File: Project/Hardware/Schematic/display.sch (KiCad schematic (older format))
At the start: 0 parts

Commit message: Skapade LCD symbol och lade till display-krets.
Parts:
- added C?: 2.2u, symbol Device:C
- added LCD?: DEM16228SBH-PW-N, symbol PASC:DEM16228SBH-PW-N
- added Q?: BSS138, Package_TO_SOT_SMD:SOT-23, symbol Transistor_FET:BSS138
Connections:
- net labels added: +5V, GND, LCD_BACKLIGHT, LCD_CONTRAST, LCD_DB0, LCD_DB1, LCD_DB2, LCD_DB3, LCD_DB4, LCD_DB5, LCD_DB6, LCD_DB7, LCD_E, LCD_RS, LCD_RW, LCD_VDD, LCD_VLED, LCD_VSS
- wire segments 0 -> 8
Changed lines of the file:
@@
 EELAYER 26 0
 EELAYER END
-$Descr A4 11693 8268
+$Descr User 5906 5906
 encoding utf-8
-Sheet 1 7
+Sheet 5 7
 Title ""
 Date ""
@@
 Comment4 ""
 $EndDescr
+$Comp
+L PASC:DEM16228SBH-PW-N LCD?
+U 1 1 5C58DC7E
+P 3600 2200
+F 0 "LCD?" H 3927 2246 50  0000 L CNN
+F 1 "DEM16228SBH-PW-N" H 3927 2155 50  0000 L CNN
+F 2 "" H 4000 2500 50  0001 C CNN
+F 3 "" H 4000 2500 50  0001 C CNN
+	1    3600 2200
+	1    0    0    -1
+$EndComp
+Text Label 3200 2900 2    50   ~ 0
+LCD_DB7
+Text Label 3200 2800 2    50   ~ 0
+LCD_DB6
+Text Label 3200 2700 2    50   ~ 0
+LCD_DB5
+Text Label 3200 2600 2    50   ~ 0
+LCD_DB4
+Text Label 3200 2500 2    50   ~ 0
+LCD_DB3
+Text Label 3200 2400 2    50   ~ 0
+LCD_DB2
+Text Label 3200 2300 2    50   ~ 0
+LCD_DB1
+Text Label 3200 2200 2    50   ~ 0
+LCD_DB0
+Text Label 3200 2100 2    50   ~ 0
+LCD_E
+Text Label 3200 2000 2    50   ~ 0
+LCD_RW
+Text Label 3200 1900 2    50   ~ 0
+LCD_RS
+Text Label 3200 1800 2    50   ~ 0
+LCD_CONTRAST
+$Comp
+L power:+5V #PWR?
+U 1 1 5C58DDEB
+P 1800 1500
+F 0 "#PWR?" H 1800 1350 50  0001 C CNN
+F 1 "+5V" H 1815 1673 50  0000 C CNN
+F 2 "" H 1800 1500 50  0001 C CNN
+F 3 "" H 1800 1500 50  0001 C CNN
+	1    1800 1500
+	1    0    0    -1
+$EndComp
+$Comp
+L power:GND #PWR?
+U 1 1 5C58DE2B
+P 1800 2100
+F 0 "#PWR?" H 1800 1850 50  0001 C CNN
+F 1 "GND" H 1805 1927 50  0000 C CNN
+F 2 "" H 1800 2100 50  0001 C CNN
+F 3 "" H 1800 2100 50  0001 C CNN
+	1    1800 2100
+	1    0    0    -1
+$EndComp
+Text Label 3200 1700 2    50   ~ 0
+LCD_VDD
+Text Label 3200 1600 2    50   ~ 0
+LCD_VSS
+Text Label 3200 1500 2    50   ~ 0
+LCD_VLED
+$Comp
+L Device:C C?
+U 1 1 5C58DF2A
+P 1800 1800
+F 0 "C?" H 1915 1846 50  0000 L CNN
+F 1 "2.2u" H 1915 1755 50  0000 L CNN
+F 2 "" H 1838 1650 50  0001 C CNN
+F 3 "~" H 1800 1800 50  0001 C CNN
+	1    1800 1800
+	1    0    0    -1
+$EndComp
+Wire Wire Line
+	1800 1650 1800 1600
+Wire Wire Line
+	1800 1950 1800 2000
+Wire Wire Line
+	1800 1600 2000 1600
+Connection ~ 1800 1600
+Wire Wire Line
+	1800 1600 1800 1500
+Wire Wire Line
+	1800 2000 2000 2000
+Connection ~ 1800 2000
+Wire Wire Line
+	1800 2000 1800 2100
+Text Label 2000 1600 0    50   ~ 0
+LCD_VDD
+Text Label 2000 2000 0    50   ~ 0
+LCD_VSS
+$Comp
+L Transistor_FET:BSS138 Q?
+U 1 1 5C58DFD0
+P 1700 3000
+F 0 "Q?" H 1905 3046 50  0000 L CNN
+F 1 "BSS138" H 1905 2955 50  0000 L CNN
+F 2 "Package_TO_SOT_SMD:SOT-23" H 1900 2925 50  0001 L CIN
+F 3 "https://www.fairchildsemi.com/datasheets/BS/BSS138.pdf" H 1700 3000 50  0001 L CNN
+	1    1700 3000
+	1    0    0    -1
+$EndComp
+Text Label 1500 3000 2    50   ~ 0
+LCD_BACKLIGHT
+$Comp
+L power:GND #PWR?
+U 1 1 5C58E03F
+P 1800 3300
+F 0 "#PWR?" H 1800 3050 50  0001 C CNN
+F 1 "GND" H 1805 3127 50  0000 C CNN
+F 2 "" H 1800 3300 50  0001 C CNN
+F 3 "" H 1800 3300 50  0001 C CNN
+	1    1800 3300
+	1    0    0    -1
+$EndComp
+Wire Wire Line
+	1800 2800 1800 2700
+Text Label 1800 2700 0    50   ~ 0
+LCD_VLED
+Wire Wire Line
+	1800 3200 1800 3300
 $EndSCHEMATC

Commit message: Lade till gate-resistor till LCD-backlight FETen.
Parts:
- added R?: 100, symbol Device:R
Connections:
- wire segments 8 -> 10
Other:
- moved on the sheet: Q?
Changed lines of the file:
@@
 L Transistor_FET:BSS138 Q?
 U 1 1 5C58DFD0
-P 1700 3000
-F 0 "Q?" H 1905 3046 50  0000 L CNN
-F 1 "BSS138" H 1905 2955 50  0000 L CNN
-F 2 "Package_TO_SOT_SMD:SOT-23" H 1900 2925 50  0001 L CIN
-F 3 "https://www.fairchildsemi.com/datasheets/BS/BSS138.pdf" H 1700 3000 50  0001 L CNN
-	1    1700 3000
+P 2000 3000
+F 0 "Q?" H 2205 3046 50  0000 L CNN
+F 1 "BSS138" H 2205 2955 50  0000 L CNN
+F 2 "Package_TO_SOT_SMD:SOT-23" H 2200 2925 50  0001 L CIN
+F 3 "https://www.fairchildsemi.com/datasheets/BS/BSS138.pdf" H 2000 3000 50  0001 L CNN
+	1    2000 3000
 	1    0    0    -1
 $EndComp
-Text Label 1500 3000 2    50   ~ 0
+Text Label 1400 3000 2    50   ~ 0
 LCD_BACKLIGHT
 $Comp
 L power:GND #PWR?
 U 1 1 5C58E03F
-P 1800 3300
-F 0 "#PWR?" H 1800 3050 50  0001 C CNN
-F 1 "GND" H 1805 3127 50  0000 C CNN
-F 2 "" H 1800 3300 50  0001 C CNN
-F 3 "" H 1800 3300 50  0001 C CNN
-	1    1800 3300
+P 2100 3300
+F 0 "#PWR?" H 2100 3050 50  0001 C CNN
+F 1 "GND" H 2105 3127 50  0000 C CNN
+F 2 "" H 2100 3300 50  0001 C CNN
+F 3 "" H 2100 3300 50  0001 C CNN
+	1    2100 3300
 	1    0    0    -1
 $EndComp
 Wire Wire Line
-	1800 2800 1800 2700
-Text Label 1800 2700 0    50   ~ 0
+	2100 2800 2100 2700
+Text Label 2100 2700 0    50   ~ 0
 LCD_VLED
 Wire Wire Line
-	1800 3200 1800 3300
+	2100 3200 2100 3300
+$Comp
+L Device:R R?
+U 1 1 5C58E912
+P 1600 3000
+F 0 "R?" V 1500 3000 50  0000 C CNN
+F 1 "100" V 1700 3000 50  0000 C CNN
+F 2 "" V 1530 3000 50  0001 C CNN
+F 3 "~" H 1600 3000 50  0001 C CNN
+	1    1600 3000
+	0    1    1    0
+$EndComp
+Wire Wire Line
+	1800 3000 1750 3000
+Wire Wire Line
+	1450 3000 1400 3000
 $EndSCHEMATC

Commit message: La till connection stm32 till display, footprint for DEM16220 lcd
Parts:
- removed LCD?: DEM16228SBH-PW-N, symbol PASC:DEM16228SBH-PW-N
- added J?: Conn_01x16_Male, symbol Connector:Conn_01x16_Male
- added U?: DEM16220SYM, symbol PASC:DEM16220SYM
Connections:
- net labels added: LCD_VLED+, LCD_VLED-, LCS_RW, LCS_VDD, V0
- wire segments 10 -> 26
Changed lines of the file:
@@
 $EndDescr
-$Comp
-L PASC:DEM16228SBH-PW-N LCD?
-U 1 1 5C58DC7E
-P 3600 2200
-F 0 "LCD?" H 3927 2246 50  0000 L CNN
-F 1 "DEM16228SBH-PW-N" H 3927 2155 50  0000 L CNN
-F 2 "" H 4000 2500 50  0001 C CNN
-F 3 "" H 4000 2500 50  0001 C CNN
-	1    3600 2200
-	1    0    0    -1
-$EndComp
-Text Label 3200 2900 2    50   ~ 0
-LCD_DB7
-Text Label 3200 2800 2    50   ~ 0
-LCD_DB6
-Text Label 3200 2700 2    50   ~ 0
-LCD_DB5
-Text Label 3200 2600 2    50   ~ 0
-LCD_DB4
-Text Label 3200 2500 2    50   ~ 0
-LCD_DB3
-Text Label 3200 2400 2    50   ~ 0
-LCD_DB2
-Text Label 3200 2300 2    50   ~ 0
-LCD_DB1
-Text Label 3200 2200 2    50   ~ 0
-LCD_DB0
-Text Label 3200 2100 2    50   ~ 0
-LCD_E
-Text Label 3200 2000 2    50   ~ 0
-LCD_RW
-Text Label 3200 1900 2    50   ~ 0
-LCD_RS
-Text Label 3200 1800 2    50   ~ 0
-LCD_CONTRAST
 $Comp
 L power:+5V #PWR?
@@
 	1    0    0    -1
 $EndComp
-Text Label 3200 1700 2    50   ~ 0
-LCD_VDD
-Text Label 3200 1600 2    50   ~ 0
-LCD_VSS
-Text Label 3200 1500 2    50   ~ 0
-LCD_VLED
 $Comp
 L Device:C C?
@@
 Wire Wire Line
 	1450 3000 1400 3000
+$Comp
+L Connector:Conn_01x16_Male J?
+U 1 1 5C69769F
+P 3200 2250
+F 0 "J?" H 3306 3128 50  0000 C CNN
+F 1 "Conn_01x16_Male" H 3306 3037 50  0000 C CNN
+F 2 "" H 3200 2250 50  0001 C CNN
+F 3 "~" H 3200 2250 50  0001 C CNN
+	1    3200 2250
+	-1   0    0    1
+$EndComp
+Wire Wire Line
+	3000 2950 2600 2950
+Text Label 2600 2950 0    50   ~ 0
+LCD_VSS
+Wire Wire Line
+	3000 2850 2600 2850
+Text Label 2600 2850 0    50   ~ 0
+LCD_VDD
+Wire Wire Line
+	3000 2750 2600 2750
+Text Label 2600 2750 0    50   ~ 0
+V0
+Wire Wire Line
+	3000 2650 2600 2650
+Text Label 2600 2650 0    50   ~ 0
+LCD_RS
+Wire Wire Line
+	3000 2550 2600 2550
+Text Label 2600 2550 0    50   ~ 0
+LCS_RW
+Wire Wire Line
+	3000 2450 2600 2450
+Text Label 2600 2450 0    50   ~ 0
+LCD_E
+Wire Wire Line
+	3000 2350 2600 2350
+Text Label 2600 2350 0    50   ~ 0
+LCD_DB0
+Wire Wire Line
+	3000 2250 2600 2250
+Text Label 2600 2250 0    50   ~ 0
+LCD_DB1
+Wire Wire Line
+	3000 2150 2600 2150
+Text Label 2600 2150 0    50   ~ 0
+LCD_DB2
+Wire Wire Line
+	3000 2050 2600 2050
+Text Label 2600 2050 0    50   ~ 0
+LCD_DB3
+Wire Wire Line
+	3000 1950 2600 1950
+Text Label 2600 1950 0    50   ~ 0
+LCD_DB4
+Wire Wire Line
+	3000 1850 2600 1850
+Text Label 2600 1850 0    50   ~ 0
+LCD_DB5
+Wire Wire Line
+	3000 1750 2600 1750
+Text Label 2600 1750 0    50   ~ 0
+LCD_DB6
+Wire Wire Line
+	3000 1650 2600 1650
+Text Label 2600 1650 0    50   ~ 0
+LCD_DB7
+Wire Wire Line
+	3000 1550 2600 1550
+Wire Wire Line
+	3000 1450 2600 1450
+Text Label 2600 1550 0    50   ~ 0
+LCD_VLED+
+Text Label 2600 1450 0    50   ~ 0
+LCD_VLED-
+$Comp
+L PASC:DEM16220SYM U?
+U 1 1 5C69A8D5
+P 4500 2000
+F 0 "U?" H 4827 1946 50  0000 L CNN
+F 1 "DEM16220SYM" H 4827 1855 50  0000 L CNN
+F 2 "" H 4500 2000 50  0001 C CNN
+F 3 "" H 4500 2000 50  0001 C CNN
+	1    4500 2000
+	1    0    0    -1
+$EndComp
+Text Label 4100 1350 2    50   ~ 0
+LCD_VSS
+Text Label 4100 1450 2    50   ~ 0
+LCS_VDD
+Text Label 4100 1550 2    50   ~ 0
+LCD_CONTRAST
+Text Label 4100 1650 2    50   ~ 0
+LCD_RS
+Text Label 4100 1750 2    50   ~ 0
+LCD_RW
+Text Label 4100 1850 2    50   ~ 0
+LCD_E
+Text Label 4100 1950 2    50   ~ 0
+LCD_DB0
+Text Label 4100 2050 2    50   ~ 0
+LCD_DB1
+Text Label 4100 2150 2    50   ~ 0
+LCD_DB2
+Text Label 4100 2250 2    50   ~ 0
+LCD_DB3
+Text Label 4100 2350 2    50   ~ 0
+LCD_DB4
+Text Label 4100 2450 2    50   ~ 0
+LCD_DB5
+Text Label 4100 2550 2    50   ~ 0
+LCD_DB6
+Text Label 4100 2650 2    50   ~ 0
+LCD_DB7
+Text Label 4100 2800 2    50   ~ 0
+LCD_VLED+
+Text Label 4100 2900 2    50   ~ 0
+LCD_VLED-
 $EndSCHEMATC

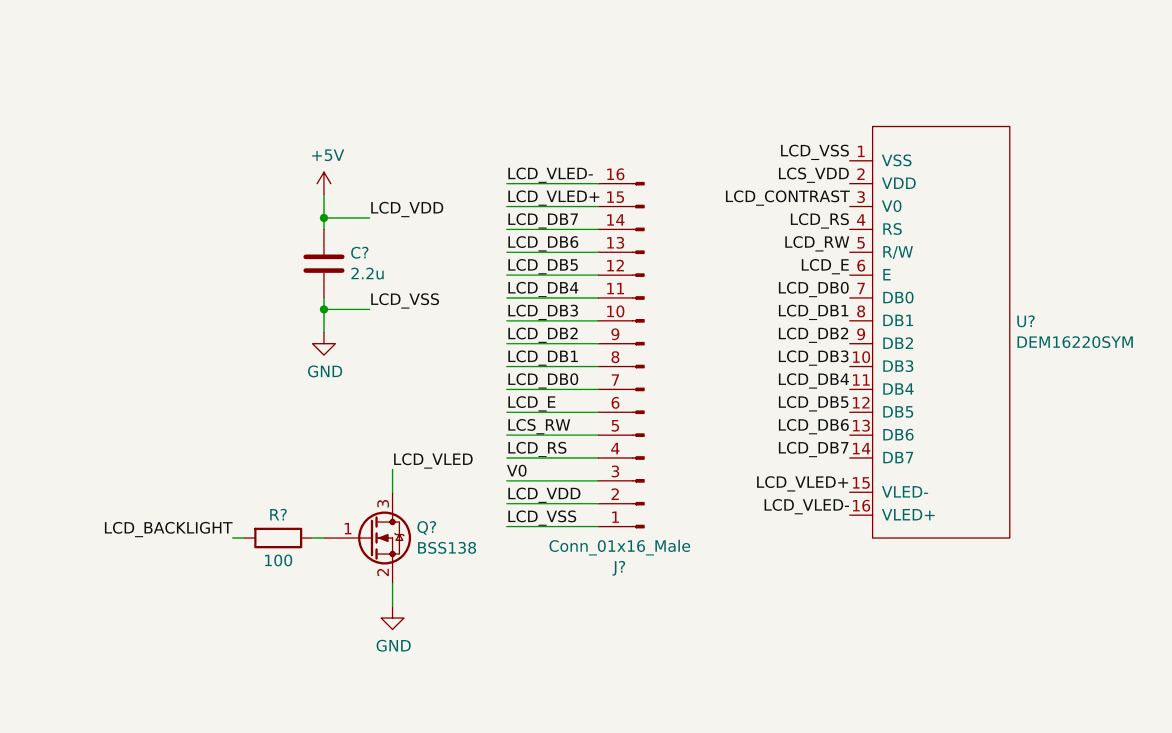
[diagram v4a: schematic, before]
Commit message: Ändrade i display: lade till LED-kontroll, bytte plats på LED- LED+ utifrån databladet.
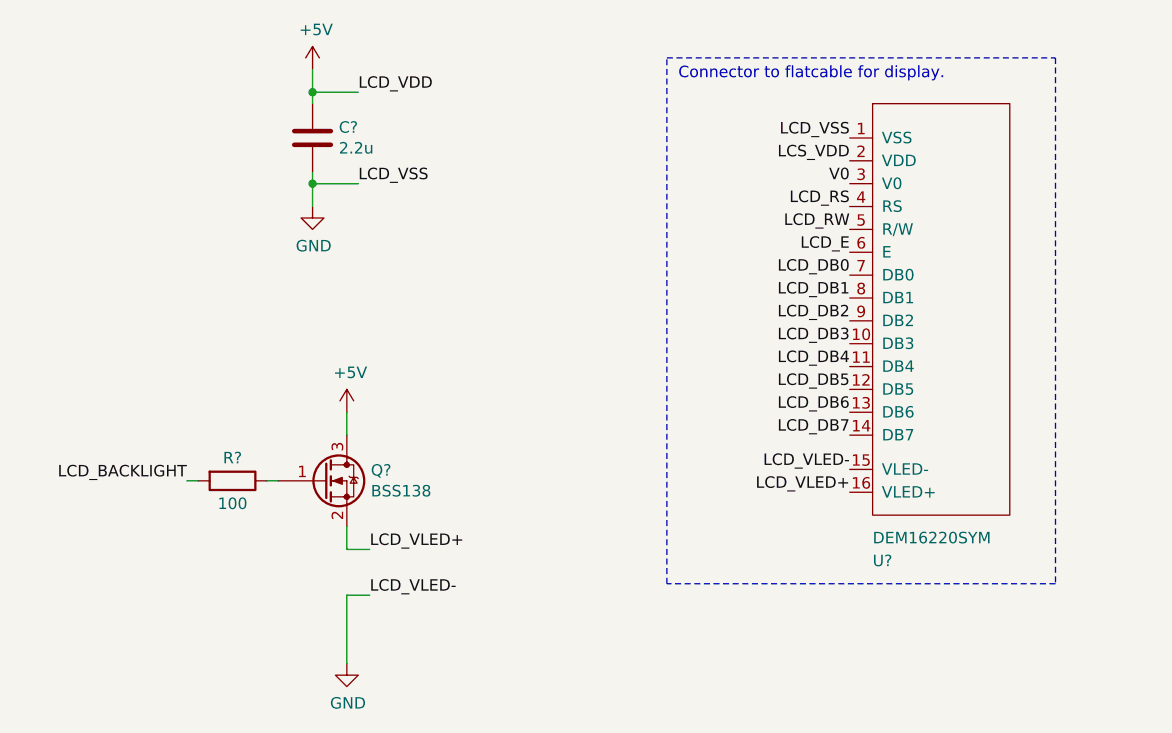
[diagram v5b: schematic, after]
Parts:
- removed J?: Conn_01x16_Male, symbol Connector:Conn_01x16_Male
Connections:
- net LCD_CONTRAST is gone; now on net V0: U?.3 (V0)
- net LCD_VLED is gone; now on net +5V: Q?.3 (D)
- net LCD_VLED- is gone; now on net LCD_VLED+: U?.16 (VLED+)
- net GND: now also U?.15 (VLED-); no longer Q?.2 (S)
- net LCD_VLED+: now also Q?.2 (S); no longer U?.15 (VLED-)
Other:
- note added: "Connector to flatcable for display."
- moved on the sheet: C?, Q?, R?, U?
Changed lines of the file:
@@
 L power:+5V #PWR?
 U 1 1 5C58DDEB
-P 1800 1500
-F 0 "#PWR?" H 1800 1350 50  0001 C CNN
-F 1 "+5V" H 1815 1673 50  0000 C CNN
-F 2 "" H 1800 1500 50  0001 C CNN
-F 3 "" H 1800 1500 50  0001 C CNN
-	1    1800 1500
+P 1750 950
+F 0 "#PWR?" H 1750 800 50  0001 C CNN
+F 1 "+5V" H 1765 1123 50  0000 C CNN
+F 2 "" H 1750 950 50  0001 C CNN
+F 3 "" H 1750 950 50  0001 C CNN
+	1    1750 950
 	1    0    0    -1
 $EndComp
@@
 L power:GND #PWR?
 U 1 1 5C58DE2B
-P 1800 2100
-F 0 "#PWR?" H 1800 1850 50  0001 C CNN
-F 1 "GND" H 1805 1927 50  0000 C CNN
-F 2 "" H 1800 2100 50  0001 C CNN
-F 3 "" H 1800 2100 50  0001 C CNN
-	1    1800 2100
+P 1750 1550
+F 0 "#PWR?" H 1750 1300 50  0001 C CNN
+F 1 "GND" H 1755 1377 50  0000 C CNN
+F 2 "" H 1750 1550 50  0001 C CNN
+F 3 "" H 1750 1550 50  0001 C CNN
+	1    1750 1550
 	1    0    0    -1
 $EndComp
@@
 L Device:C C?
 U 1 1 5C58DF2A
-P 1800 1800
-F 0 "C?" H 1915 1846 50  0000 L CNN
-F 1 "2.2u" H 1915 1755 50  0000 L CNN
-F 2 "" H 1838 1650 50  0001 C CNN
-F 3 "~" H 1800 1800 50  0001 C CNN
-	1    1800 1800
+P 1750 1250
+F 0 "C?" H 1865 1296 50  0000 L CNN
+F 1 "2.2u" H 1865 1205 50  0000 L CNN
+F 2 "" H 1788 1100 50  0001 C CNN
+F 3 "~" H 1750 1250 50  0001 C CNN
+	1    1750 1250
 	1    0    0    -1
 $EndComp
 Wire Wire Line
-	1800 1650 1800 1600
+	1750 1100 1750 1050
 Wire Wire Line
-	1800 1950 1800 2000
+	1750 1400 1750 1450
 Wire Wire Line
-	1800 1600 2000 1600
-Connection ~ 1800 1600
+	1750 1050 1950 1050
+Connection ~ 1750 1050
 Wire Wire Line
-	1800 1600 1800 1500
+	1750 1050 1750 950
 Wire Wire Line
-	1800 2000 2000 2000
-Connection ~ 1800 2000
+	1750 1450 1950 1450
+Connection ~ 1750 1450
 Wire Wire Line
-	1800 2000 1800 2100
-Text Label 2000 1600 0    50   ~ 0
+	1750 1450 1750 1550
+Text Label 1950 1050 0    50   ~ 0
 LCD_VDD
-Text Label 2000 2000 0    50   ~ 0
+Text Label 1950 1450 0    50   ~ 0
 LCD_VSS
 $Comp
 L Transistor_FET:BSS138 Q?
 U 1 1 5C58DFD0
-P 2000 3000
-F 0 "Q?" H 2205 3046 50  0000 L CNN
-F 1 "BSS138" H 2205 2955 50  0000 L CNN
-F 2 "Package_TO_SOT_SMD:SOT-23" H 2200 2925 50  0001 L CIN
-F 3 "https://www.fairchildsemi.com/datasheets/BS/BSS138.pdf" H 2000 3000 50  0001 L CNN
-	1    2000 3000
+P 1800 2750
+F 0 "Q?" H 2005 2796 50  0000 L CNN
+F 1 "BSS138" H 2005 2705 50  0000 L CNN
+F 2 "Package_TO_SOT_SMD:SOT-23" H 2000 2675 50  0001 L CIN
+F 3 "https://www.fairchildsemi.com/datasheets/BS/BSS138.pdf" H 1800 2750 50  0001 L CNN
+	1    1800 2750
 	1    0    0    -1
 $EndComp
-Text Label 1400 3000 2    50   ~ 0
+Text Label 1200 2750 2    50   ~ 0
 LCD_BACKLIGHT
+Wire Wire Line
+	1900 2550 1900 2450
+Wire Wire Line
+	1900 2950 1900 3050
 $Comp
-L power:GND #PWR?
-U 1 1 5C58E03F
-P 2100 3300
-F 0 "#PWR?" H 2100 3050 50  0001 C CNN
-F 1 "GND" H 2105 3127 50  0000 C CNN
-F 2 "" H 2100 3300 50  0001 C CNN
-F 3 "" H 2100 3300 50  0001 C CNN
-	1    2100 3300
+L Device:R R?
+U 1 1 5C58E912
+P 1400 2750
+F 0 "R?" V 1300 2750 50  0000 C CNN
+F 1 "100" V 1500 2750 50  0000 C CNN
+F 2 "" V 1330 2750 50  0001 C CNN
+F 3 "~" H 1400 2750 50  0001 C CNN
+	1    1400 2750
+	0    1    1    0
+$EndComp
+Wire Wire Line
+	1600 2750 1550 2750
+Wire Wire Line
+	1250 2750 1200 2750
+$Comp
+L PASC:DEM16220SYM U?
+U 1 1 5C69A8D5
+P 4500 1900
+F 0 "U?" H 4200 700 50  0000 L CNN
+F 1 "DEM16220SYM" H 4200 800 50  0000 L CNN
+F 2 "" H 4500 1900 50  0001 C CNN
+F 3 "" H 4500 1900 50  0001 C CNN
+	1    4500 1900
+	1    0    0    -1
+$EndComp
+Text Label 4100 1250 2    50   ~ 0
+LCD_VSS
+Text Label 4100 1350 2    50   ~ 0
+LCS_VDD
+Text Label 4100 1550 2    50   ~ 0
+LCD_RS
+Text Label 4100 1650 2    50   ~ 0
+LCD_RW
+Text Label 4100 1750 2    50   ~ 0
+LCD_E
+Text Label 4100 1850 2    50   ~ 0
+LCD_DB0
+Text Label 4100 1950 2    50   ~ 0
+LCD_DB1
+Text Label 4100 2050 2    50   ~ 0
+LCD_DB2
+Text Label 4100 2150 2    50   ~ 0
+LCD_DB3
+Text Label 4100 2250 2    50   ~ 0
+LCD_DB4
+Text Label 4100 2350 2    50   ~ 0
+LCD_DB5
+Text Label 4100 2450 2    50   ~ 0
+LCD_DB6
+Text Label 4100 2550 2    50   ~ 0
+LCD_DB7
+Text Label 4100 2800 2    50   ~ 0
+LCD_VLED+
+Text Label 4100 2700 2    50   ~ 0
+LCD_VLED-
+$Comp
+L power:+5V #PWR?
+U 1 1 5C5BE7E6
+P 1900 2450
+F 0 "#PWR?" H 1900 2300 50  0001 C CNN
+F 1 "+5V" H 1915 2623 50  0000 C CNN
+F 2 "" H 1900 2450 50  0001 C CNN
+F 3 "" H 1900 2450 50  0001 C CNN
+	1    1900 2450
 	1    0    0    -1
 $EndComp
 Wire Wire Line
-	2100 2800 2100 2700
-Text Label 2100 2700 0    50   ~ 0
-LCD_VLED
+	1900 3050 2000 3050
+Text Label 2000 3050 0    50   ~ 0
+LCD_VLED+
+Text Label 2000 3250 0    50   ~ 0
+LCD_VLED-
 Wire Wire Line
-	2100 3200 2100 3300
+	1900 3250 2000 3250
 $Comp
-L Device:R R?
-U 1 1 5C58E912
-P 1600 3000
-F 0 "R?" V 1500 3000 50  0000 C CNN
-F 1 "100" V 1700 3000 50  0000 C CNN
-F 2 "" V 1530 3000 50  0001 C CNN
-F 3 "~" H 1600 3000 50  0001 C CNN
-	1    1600 3000
-	0    1    1    0
+L power:GND #PWR?
+U 1 1 5C5BF407
+P 1900 3550
+F 0 "#PWR?" H 1900 3300 50  0001 C CNN
+F 1 "GND" H 1905 3377 50  0000 C CNN
+F 2 "" H 1900 3550 50  0001 C CNN
+F 3 "" H 1900 3550 50  0001 C CNN
+	1    1900 3550
+	1    0    0    -1
 $EndComp
-Wire Wire Line
-	1800 3000 1750 3000
-Wire Wire Line
-	1450 3000 1400 3000
-$Comp
-L Connector:Conn_01x16_Male J?
-U 1 1 5C69769F
-P 3200 2250
-F 0 "J?" H 3306 3128 50  0000 C CNN
-F 1 "Conn_01x16_Male" H 3306 3037 50  0000 C CNN
-F 2 "" H 3200 2250 50  0001 C CNN
-F 3 "~" H 3200 2250 50  0001 C CNN
-	1    3200 2250
-	-1   0    0    1
-$EndComp
-Wire Wire Line
-	3000 2950 2600 2950
-Text Label 2600 2950 0    50   ~ 0
-LCD_VSS
-Wire Wire Line
-	3000 2850 2600 2850
-Text Label 2600 2850 0    50   ~ 0
-LCD_VDD
-Wire Wire Line
-	3000 2750 2600 2750
-Text Label 2600 2750 0    50   ~ 0
+Text Label 4100 1450 2    50   ~ 0
 V0
 Wire Wire Line
-	3000 2650 2600 2650
-Text Label 2600 2650 0    50   ~ 0
-LCD_RS
-Wire Wire Line
-	3000 2550 2600 2550
-Text Label 2600 2550 0    50   ~ 0
-LCS_RW
-Wire Wire Line
-	3000 2450 2600 2450
-Text Label 2600 2450 0    50   ~ 0
-LCD_E
-Wire Wire Line
-	3000 2350 2600 2350
-Text Label 2600 2350 0    50   ~ 0
-LCD_DB0
-Wire Wire Line
-	3000 2250 2600 2250
-Text Label 2600 2250 0    50   ~ 0
-LCD_DB1
-Wire Wire Line
-	3000 2150 2600 2150
-Text Label 2600 2150 0    50   ~ 0
-LCD_DB2
-Wire Wire Line
-	3000 2050 2600 2050
-Text Label 2600 2050 0    50   ~ 0
-LCD_DB3
-Wire Wire Line
-	3000 1950 2600 1950
-Text Label 2600 1950 0    50   ~ 0
-LCD_DB4
-Wire Wire Line
-	3000 1850 2600 1850
-Text Label 2600 1850 0    50   ~ 0
-LCD_DB5
-Wire Wire Line
-	3000 1750 2600 1750
-Text Label 2600 1750 0    50   ~ 0
-LCD_DB6
-Wire Wire Line
-	3000 1650 2600 1650
-Text Label 2600 1650 0    50   ~ 0
-LCD_DB7
-Wire Wire Line
-	3000 1550 2600 1550
-Wire Wire Line
-	3000 1450 2600 1450
-Text Label 2600 1550 0    50   ~ 0
-LCD_VLED+
-Text Label 2600 1450 0    50   ~ 0
-LCD_VLED-
-$Comp
-L PASC:DEM16220SYM U?
-U 1 1 5C69A8D5
-P 4500 2000
-F 0 "U?" H 4827 1946 50  0000 L CNN
-F 1 "DEM16220SYM" H 4827 1855 50  0000 L CNN
-F 2 "" H 4500 2000 50  0001 C CNN
-F 3 "" H 4500 2000 50  0001 C CNN
-	1    4500 2000
-	1    0    0    -1
-$EndComp
-Text Label 4100 1350 2    50   ~ 0
-LCD_VSS
-Text Label 4100 1450 2    50   ~ 0
-LCS_VDD
-Text Label 4100 1550 2    50   ~ 0
-LCD_CONTRAST
-Text Label 4100 1650 2    50   ~ 0
-LCD_RS
-Text Label 4100 1750 2    50   ~ 0
-LCD_RW
-Text Label 4100 1850 2    50   ~ 0
-LCD_E
-Text Label 4100 1950 2    50   ~ 0
-LCD_DB0
-Text Label 4100 2050 2    50   ~ 0
-LCD_DB1
-Text Label 4100 2150 2    50   ~ 0
-LCD_DB2
-Text Label 4100 2250 2    50   ~ 0
-LCD_DB3
-Text Label 4100 2350 2    50   ~ 0
-LCD_DB4
-Text Label 4100 2450 2    50   ~ 0
-LCD_DB5
-Text Label 4100 2550 2    50   ~ 0
-LCD_DB6
-Text Label 4100 2650 2    50   ~ 0
-LCD_DB7
-Text Label 4100 2800 2    50   ~ 0
-LCD_VLED+
-Text Label 4100 2900 2    50   ~ 0
-LCD_VLED-
+	1900 3250 1900 3550
+Text Notes 3350 1000 0    50   ~ 0
+Connector to flatcable for display.
+Wire Notes Line
+	3300 900  5000 900
+Wire Notes Line
+	5000 900  5000 3200
+Wire Notes Line
+	5000 3200 3300 3200
+Wire Notes Line
+	3300 3200 3300 900
 $EndSCHEMATC
